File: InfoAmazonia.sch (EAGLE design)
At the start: 73 parts, among them IC1 LM2662, IC11 74HC4051, IC2 ADAFRUIT FONA, IC3 MIC29302AWD, IC4 4050D, IC5 TL032C, IC6 CA3140AM Z, IC7 TL081BCDG4, IC8 SHT20, IC9 NE555, J1 BNCPTH, J2 BNCPTH, J3 BNCPTH, U1 ARDUINO-MEGAPRO, U2 MPL3115A2, U3 USD-SOCKETNEW, U4 ALS-PT19

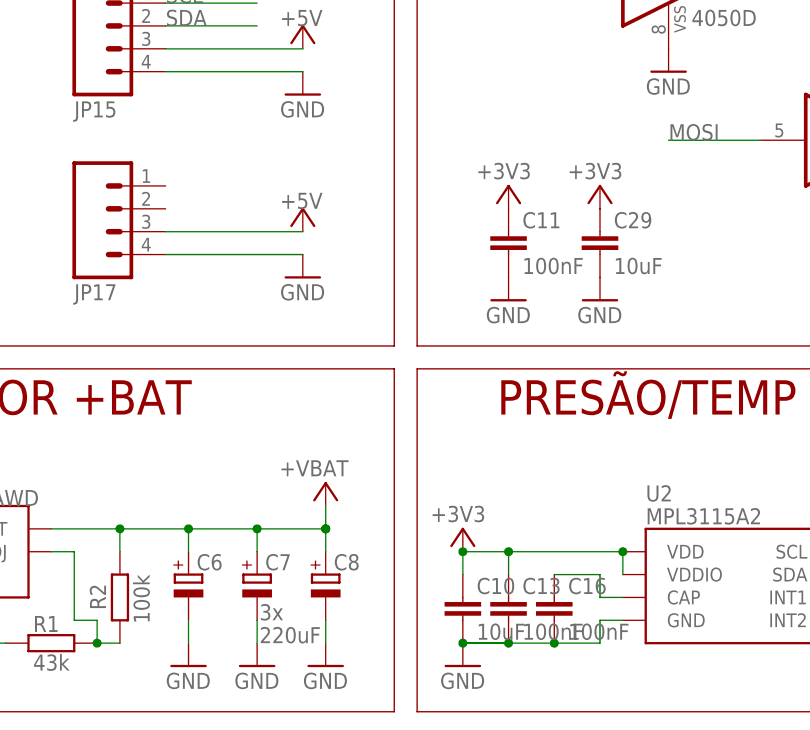
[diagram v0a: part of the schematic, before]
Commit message: - Coloquei os sensores pro lado
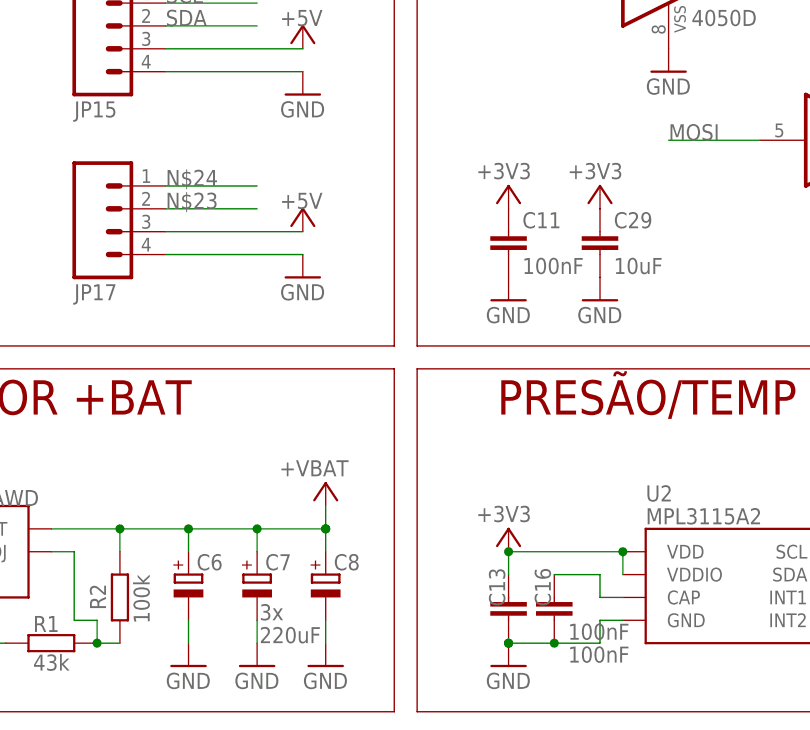
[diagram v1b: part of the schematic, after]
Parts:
- removed C10: 10uF, InfoAmazonia:C-EUC0603
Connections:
- new net N$23: JP17.2
- new net N$24: JP17.1
- net +3V3: no longer C10.1
- net GND: no longer C10.2
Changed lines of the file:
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@@
 <part name="IC2" library="InfoAmazonia" deviceset="ADAFRUIT_FONA" device="" value="ADAFRUIT FONA"/>
 <part name="+3V32" library="InfoAmazonia" deviceset="+3V3" device=""/>
-<part name="C10" library="InfoAmazonia" deviceset="C-EU" device="C0603" value="10uF"/>
 <part name="C13" library="InfoAmazonia" deviceset="C-EU" device="C0603" value="100nF"/>
 <part name="C16" library="InfoAmazonia" deviceset="C-EU" device="C0603" value="100nF"/>
@@
 <attribute name="NAME" x="-15.24" y="-45.974" size="1.778" layer="95" rot="MR180"/>
 </instance>
-<instance part="+3V32" gate="G$1" x="121.92" y="-106.68" smashed="yes">
-<attribute name="VALUE" x="124.46" y="-104.14" size="1.778" layer="96" rot="R180"/>
-</instance>
-<instance part="C10" gate="G$1" x="121.92" y="-114.3" smashed="yes">
-<attribute name="NAME" x="123.444" y="-113.919" size="1.778" layer="95"/>
-<attribute name="VALUE" x="123.444" y="-118.999" size="1.778" layer="96"/>
+<instance part="+3V32" gate="G$1" x="127" y="-106.68" smashed="yes">
+<attribute name="VALUE" x="129.54" y="-104.14" size="1.778" layer="96" rot="R180"/>
 </instance>
 <instance part="C13" gate="G$1" x="127" y="-114.3" smashed="yes">
-<attribute name="NAME" x="128.524" y="-113.919" size="1.778" layer="95"/>
-<attribute name="VALUE" x="128.524" y="-118.999" size="1.778" layer="96"/>
+<attribute name="NAME" x="126.619" y="-115.316" size="1.778" layer="95" rot="R90"/>
+<attribute name="VALUE" x="133.604" y="-121.539" size="1.778" layer="96"/>
 </instance>
 <instance part="C16" gate="G$1" x="132.08" y="-114.3" smashed="yes">
-<attribute name="NAME" x="133.604" y="-113.919" size="1.778" layer="95"/>
+<attribute name="NAME" x="131.699" y="-115.316" size="1.778" layer="95" rot="R90"/>
 <attribute name="VALUE" x="133.604" y="-118.999" size="1.778" layer="96"/>
 </instance>
-<instance part="GND13" gate="1" x="121.92" y="-121.92" smashed="yes">
-<attribute name="VALUE" x="119.38" y="-124.46" size="1.778" layer="96"/>
+<instance part="GND13" gate="1" x="127" y="-121.92" smashed="yes">
+<attribute name="VALUE" x="124.46" y="-124.46" size="1.778" layer="96"/>
 </instance>
 <instance part="U2" gate="G$1" x="152.4" y="-111.76" smashed="yes">
@@
 <wire x1="137.16" y1="-119.38" x2="132.08" y2="-119.38" width="0.1524" layer="91"/>
 <pinref part="U2" gate="G$1" pin="GND"/>
-<junction x="121.92" y="-119.38"/>
+<junction x="127" y="-119.38"/>
 <pinref part="GND13" gate="1" pin="GND"/>
-<pinref part="C10" gate="G$1" pin="2"/>
 <pinref part="C13" gate="G$1" pin="2"/>
 <junction x="127" y="-119.38"/>
-<wire x1="127" y1="-119.38" x2="121.92" y2="-119.38" width="0.1524" layer="91"/>
-<wire x1="121.92" y1="-119.38" x2="132.08" y2="-119.38" width="0.1524" layer="91"/>
+<wire x1="127" y1="-119.38" x2="132.08" y2="-119.38" width="0.1524" layer="91"/>
 <junction x="132.08" y="-119.38"/>
 </segment>
@@
 <wire x1="139.7" y1="-109.22" x2="127" y2="-109.22" width="0.1524" layer="91"/>
 <pinref part="+3V32" gate="G$1" pin="+3V3"/>
-<pinref part="C10" gate="G$1" pin="1"/>
-<wire x1="127" y1="-109.22" x2="121.92" y2="-109.22" width="0.1524" layer="91"/>
-<wire x1="121.92" y1="-111.76" x2="121.92" y2="-109.22" width="0.1524" layer="91"/>
 <pinref part="C13" gate="G$1" pin="1"/>
 <wire x1="127" y1="-111.76" x2="127" y2="-109.22" width="0.1524" layer="91"/>
-<junction x="121.92" y="-109.22"/>
 <junction x="127" y="-109.22"/>
 <junction x="139.7" y="-109.22"/>
@@
 </segment>
 </net>
+<net name="N$23" class="0">
+<segment>
+<pinref part="JP17" gate="G$1" pin="2"/>
+<wire x1="88.9" y1="-71.12" x2="99.06" y2="-71.12" width="0.1524" layer="91"/>
+<label x="88.9" y="-71.12" size="1.778" layer="95"/>
+</segment>
+</net>
+<net name="N$24" class="0">
+<segment>
+<pinref part="JP17" gate="G$1" pin="1"/>
+<wire x1="88.9" y1="-68.58" x2="99.06" y2="-68.58" width="0.1524" layer="91"/>
+<label x="88.9" y="-68.58" size="1.778" layer="95"/>
+</segment>
+</net>
